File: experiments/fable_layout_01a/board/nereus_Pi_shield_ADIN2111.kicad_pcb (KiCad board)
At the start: 6 copper layers, 46 x 65 mm, 138 parts, among them J1 Raspberry_Pi_2_3, J5 SM02B-GHS-TB, T1 74930000, T2 74930000, U1 ADIN2111BCPZ, U10 LMR51430YDDCR, U11 TPS26621DRCR, U2 AP22913CN4-7, U3 AP22913CN4-7, U4 INA232AIDDFR, U5 LMR51430YDDCR, U6 TPS62840YBGR, Y1 ABM11W-25.0000MHZ-6-K1Z-T3

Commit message: fable layout 1.a M1: placement per OPTIONS (blocks moved, LEDs north, JP1 top, strip re-ordered, B18 in the band); check_fixed 0 failures, 0 new courtyard overlaps; renders
Co-Authored-By: Claude Fable 5.1 <noreply@anthropic.com>
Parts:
- JP1: moved to F.Cu
- R41: moved to B.Cu
- moved R16 31.0 mm to (6.30, 56.0)
- moved D9 30.5 mm to (18.4, 1.40)
- moved R45 30.0 mm to (19.4, 4.20), turned to 90 degrees
- moved D8 29.3 mm to (15.0, 1.40)
- moved R46 29.1 mm to (10.8, 4.20), turned to 90 degrees
- moved R44 28.7 mm to (18.0, 4.20), turned to 90 degrees
- moved D10 28.7 mm to (11.6, 1.40)
- moved JP2 24.9 mm to (15.0, 4.30)
- moved TP38 18.9 mm to (37.0, 14.0)
- moved C58 16.9 mm to (35.0, 14.0)
- moved C31 16.2 mm to (36.6, 33.9)
- moved C29 16.2 mm to (30.4, 30.8)
- moved C30 16.2 mm to (30.3, 30.7)
- moved R20 16.2 mm to (31.2, 36.5)
- moved R22 16.2 mm to (33.4, 36.5)
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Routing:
- net GND: track 120.5 -> 0.00 mm, vias 90 -> 0
- net 3V3: track 112.0 -> 0.00 mm, vias 16 -> 0
- net /Top-Level Schematic/~{ADIN_INT}: track 48.5 -> 0.00 mm, vias 2 -> 0
- net /Top-Level Schematic/ADIN_PWR: track 46.3 -> 0.00 mm, vias 3 -> 0
- net /Top-Level Schematic/BM2_P: track 53.7 -> 11.6 mm, vias 12 -> 7
- net /Top-Level Schematic/BM1_N: track 52.9 -> 11.6 mm, vias 12 -> 7
- net /Top-Level Schematic/~{ADIN_CS}: track 41.2 -> 0.00 mm, vias 2 -> 0
- net VBUS: track 38.3 -> 0.00 mm, vias 21 -> 0
- net /Top-Level Schematic/ADIN_MISO: track 38.0 -> 0.00 mm, vias 1 -> 0
- net 1V8: track 36.7 -> 0.00 mm, vias 2 -> 0
- net /Top-Level Schematic/ADIN/~{ADIN_P2_LED1}: track 36.6 -> 0.00 mm, vias 2 -> 0
- net /Top-Level Schematic/~{PAYLOAD_FAULT}: track 36.6 -> 0.00 mm, vias 3 -> 0
- net /Top-Level Schematic/ADIN_MOSI: track 35.9 -> 0.00 mm, vias 2 -> 0
- net ADIN_VDDIO: track 35.0 -> 0.00 mm, vias 6 -> 0
- net /Top-Level Schematic/ADIN_SCK: track 32.1 -> 0.00 mm, vias 2 -> 0
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- removed copper zone on In4.Cu, net (none)
- removed copper zone on B.Cu, net /Top-Level Schematic/5V_PI
- removed copper zone on F.Cu, net /Top-Level Schematic/5V_PI
- removed copper zone on In4.Cu, net /Top-Level Schematic/ADIN/ADIN_AVDD
- removed copper zone on In4.Cu, net /Top-Level Schematic/PoDL/Power Monitor/P_IN
- removed copper zone on F.Cu, net /Top-Level Schematic/Power Regulators/3V3_Buck_SW
- removed copper zone on F.Cu, net /Top-Level Schematic/Power Regulators/5V_Buck_SW
- removed copper zone on F.Cu, net 3V3
- removed copper zone on In4.Cu, net 3V3
- removed copper zone on In4.Cu, net ADIN_VDDIO
- removed copper zone on In2.Cu, net GND
- removed copper zone on In4.Cu, net VBUS

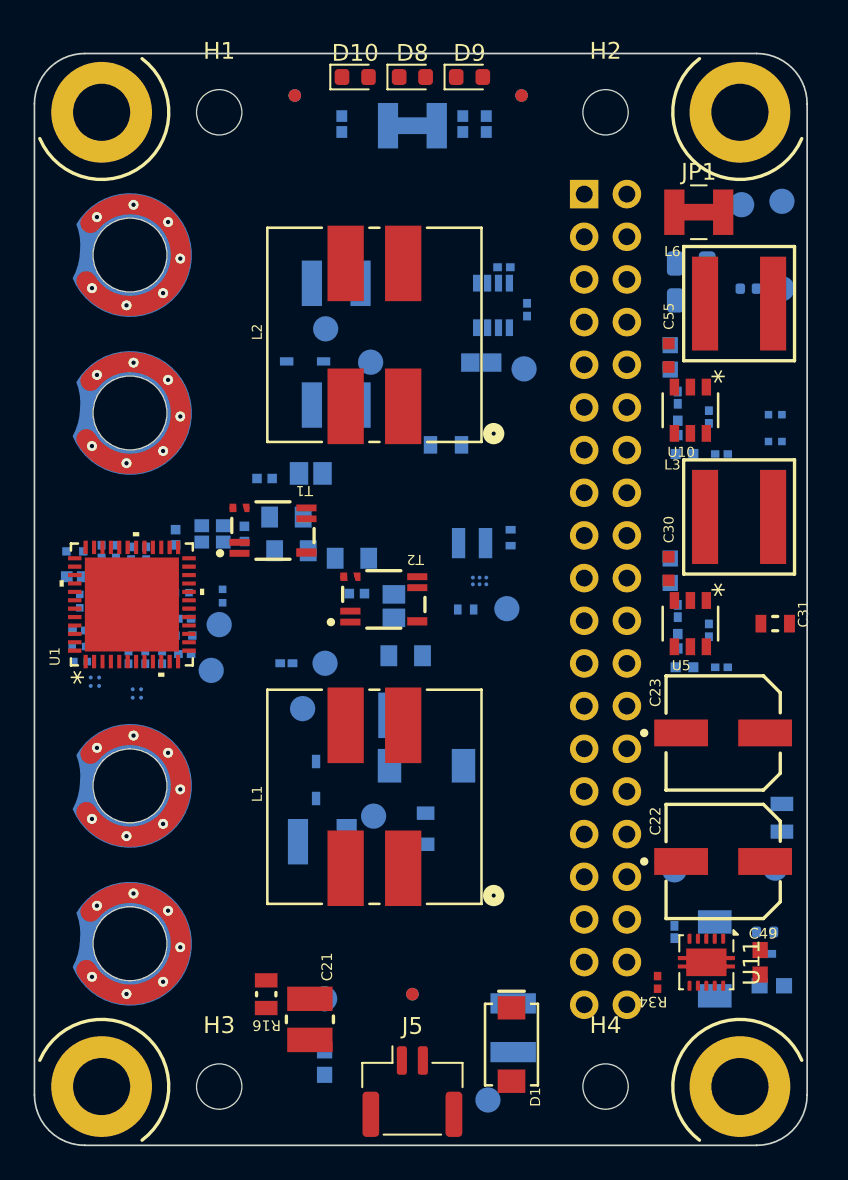
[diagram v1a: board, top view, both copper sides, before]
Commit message: fable layout 1.a M2: block copper, planes, routing — stopped short of the bar (3 open links, port-1 pair 1.2 mm over, 12 new-copper DRC errors); REPORT.md with the shortfall table
Pipeline: snapshot restarts, planes before a pre-route trim of Sofar's lead-outs, exact distance-based router maps,
pad-field escapes, no fallback classes, coupled-pair router with swap figures, bottom GND pour as the mote.
M3 (JLCPCB DFM sweep) not started: Nick asked for a wind-down after ~2 h.

Co-Authored-By: Claude Fable 5.1 <noreply@anthropic.com>
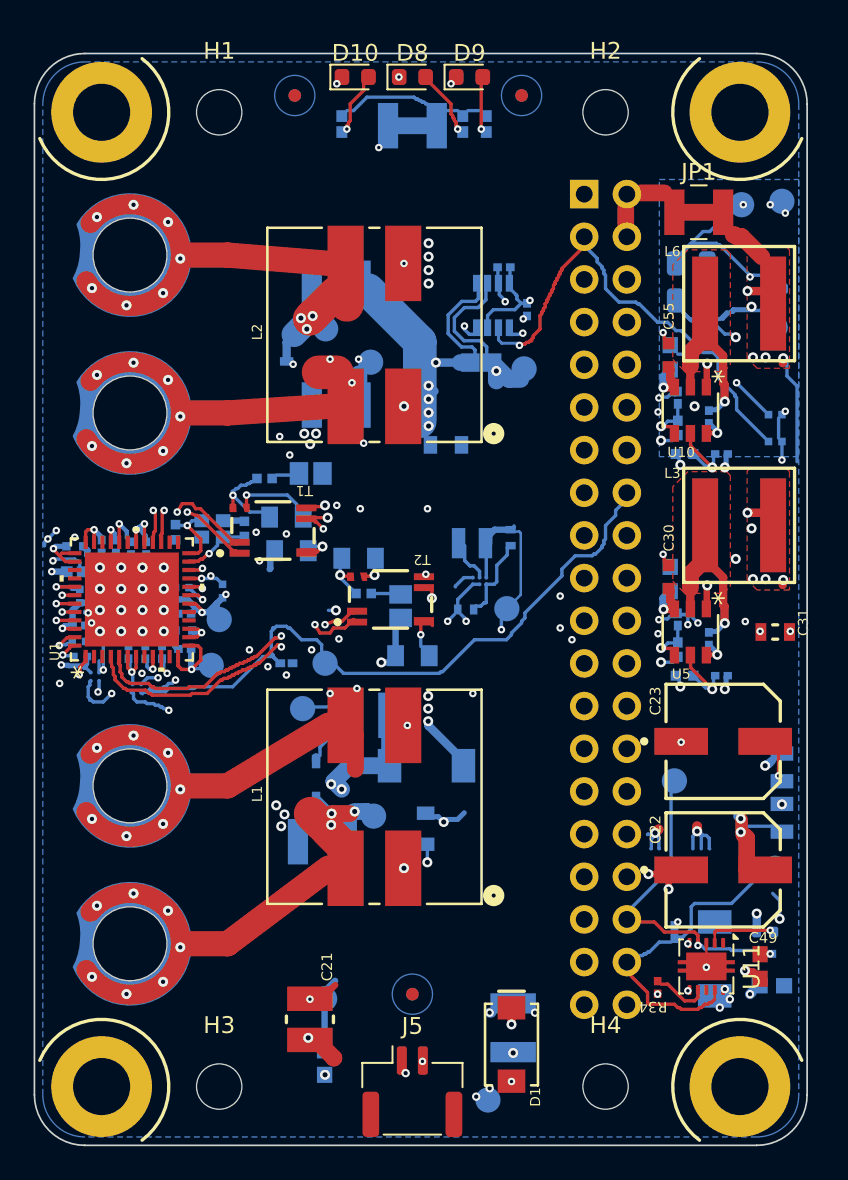
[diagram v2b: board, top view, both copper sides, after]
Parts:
- R16: moved to B.Cu
- moved R16 33.5 mm to (37.0, 42.5)
- moved TP19 5.30 mm to (30.6, 43.3)
- moved TP38 2.33 mm to (36.6, 16.3)
- moved C58 1.60 mm to (36.6, 14.0)
- moved R21 0.50 mm to (30.8, 33.7)
- moved C22 0.50 mm to (33.5, 48.6)
- moved C23 0.50 mm to (33.5, 41.0)
- moved C28 0.50 mm to (32.7, 34.8)
- moved C29 0.50 mm to (30.4, 31.3)
- moved C30 0.50 mm to (30.3, 31.2)
- moved C31 0.50 mm to (36.6, 34.4)
- moved L3 0.50 mm to (34.5, 28.1)
- moved R20 0.50 mm to (31.2, 37.0)
- moved R22 0.50 mm to (33.4, 37.0)
- moved R23 0.50 mm to (30.8, 35.5)
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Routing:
- net 3V3: track 0.00 -> 112.7 mm, vias 0 -> 20
- net GND: track 0.00 -> 108.7 mm, vias 0 -> 78
- net ADIN_VDDIO: track 0.00 -> 49.1 mm, vias 0 -> 10
- net /Top-Level Schematic/ADIN_PWR: track 0.00 -> 45.9 mm, vias 0 -> 2
- net /Top-Level Schematic/ADIN/~{ADIN_P2_LED1}: track 0.00 -> 44.5 mm, vias 0 -> 3
- net /Top-Level Schematic/BM1_N: track 11.6 -> 54.1 mm, vias 7 -> 12
- net /Top-Level Schematic/~{ADIN_CS}: track 0.00 -> 39.8 mm, vias 0 -> 2
- net /Top-Level Schematic/ADIN_MISO: track 0.00 -> 38.5 mm, vias 0 -> 1
- net /Top-Level Schematic/~{ADIN_INT}: track 0.00 -> 38.0 mm, vias 0 -> 1
- net /Top-Level Schematic/ADIN/~{ADIN_P1_LED1}: track 0.00 -> 37.6 mm, vias 0 -> 4
- net 1V8: track 0.00 -> 37.5 mm, vias 0 -> 3
- net /Top-Level Schematic/BM2_P: track 11.6 -> 48.5 mm, vias 7 -> 12
- net /Top-Level Schematic/ADIN_MOSI: track 0.00 -> 33.5 mm, vias 0 -> 2
- net /Top-Level Schematic/ADIN_SCK: track 0.00 -> 32.8 mm, vias 0 -> 3
- net VBUS: track 0.00 -> 28.9 mm, vias 0 -> 17
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- added copper zone on In4.Cu, net (none)
- added copper zone on B.Cu, net /Top-Level Schematic/5V_PI
- added copper zone on F.Cu, net /Top-Level Schematic/5V_PI
- added copper zone on In4.Cu, net /Top-Level Schematic/ADIN/ADIN_AVDD
- added copper zone on In4.Cu, net /Top-Level Schematic/PoDL/Power Monitor/P_IN
- added copper zone on F.Cu, net /Top-Level Schematic/Power Regulators/3V3_Buck_SW
- added copper zone on F.Cu, net /Top-Level Schematic/Power Regulators/5V_Buck_SW
- added copper zone on F.Cu, net 3V3
- added copper zone on In4.Cu, net 3V3
- added copper zone on In4.Cu, net ADIN_VDDIO
- added copper zone on B.Cu, net GND
- added copper zone on In2.Cu, net GND
- added copper zone on In4.Cu, net VBUS

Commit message: fable layout 1.a S2: M2 at its bar — fan-out first for U2/U3, exact via/hole checks, 5V_PI In3 patch, zone vias over other-layer copper; board + renders + review views; REPORT/LOG/HANDOFF
DRC 111 errors all Sofar-copied with reasons, 1 unconnected (J1 no-connect), 0 dangling; pairs 9.46/8.80/17.98/18.62 mm; rules 0/0/0; blockcheck 0 missing.

Co-Authored-By: Claude Fable 5.1 <noreply@anthropic.com>
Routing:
- net GND: track 108.7 -> 54.1 mm, vias 78 -> 71
- net /Top-Level Schematic/ADIN_MISO: track 38.5 -> 66.5 mm
- net /Top-Level Schematic/~{ADIN_CS}: track 39.8 -> 67.6 mm, vias 2 -> 6
- net /Top-Level Schematic/ADIN_PWR: track 45.9 -> 43.0 mm, vias 2 -> 10
- net /Top-Level Schematic/~{ADIN_INT}: track 38.0 -> 40.6 mm
- net /Top-Level Schematic/BM1_DATA_P: track 10.7 -> 9.46 mm
- net 1V8: track 37.5 -> 37.0 mm, vias 3 -> 4
- net VBUS_OUT: track 22.9 -> 23.4 mm
- net 3V3: track 112.7 -> 112.3 mm, vias 20 -> 21
- net VBUS: vias 17 -> 18
- added copper zone on In3.Cu, net /Top-Level Schematic/5V_PI
